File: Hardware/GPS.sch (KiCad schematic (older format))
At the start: 15 parts, among them Q1 IRLML6401, U1 ANTENOVA-UB

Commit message: Prepare for r2
Delete board, netlist, associations
Clear annotations
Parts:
- renumbered C7 to C?, C2 to C?, C1 to C?, C3 to C?, C5 to C?, C4 to C?, C6 to C?, FB1 to FB?, FB2 to FB?, L1 to L?, L2 to L?, Q1 to Q?, R4 to R?, R3 to R?, U1 to U?
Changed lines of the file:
@@
 $EndDescr
 $Comp
-L ANTENOVA-UB U1
+L ANTENOVA-UB U?
 U 1 1 52E9B1BE
 P 7100 4150
-F 0 "U1" H 7100 5300 60  0000 C CNN
+F 0 "U?" H 7100 5300 60  0000 C CNN
 F 1 "ANTENOVA-UB" H 7100 3000 60  0000 C CNN
 F 2 "~" H 7100 4150 60  0000 C CNN
@@
 $EndComp
 $Comp
-L C C7
+L C C?
 U 1 1 52E9B2C1
 P 7900 3450
-F 0 "C7" H 7950 3600 60  0000 L CNN
+F 0 "C?" H 7950 3600 60  0000 L CNN
 F 1 "18pF" H 7950 3300 60  0000 L CNN
 F 2 "CAPC1005-N" H 7900 3450 60  0001 C CNN
@@
 $EndComp
 $Comp
-L L L1
+L L L?
 U 1 1 52E9B2DC
 P 8350 3100
-F 0 "L1" H 8350 3000 60  0000 C CNN
+F 0 "L?" H 8350 3000 60  0000 C CNN
 F 1 "DNP" H 8350 3150 60  0000 C CNN
 F 2 "INDC1005-N" H 8350 3100 60  0001 C CNN
@@
 $EndComp
 $Comp
-L GND #PWR055
+L GND #PWR?
 U 1 1 52E9B2FA
 P 8700 3100
-F 0 "#PWR055" H 8700 3100 30  0001 C CNN
+F 0 "#PWR?" H 8700 3100 30  0001 C CNN
 F 1 "GND" H 8700 3030 30  0001 C CNN
 F 2 "" H 8700 3100 60  0000 C CNN
@@
 $EndComp
 $Comp
-L GND #PWR056
+L GND #PWR?
 U 1 1 52E9B317
 P 8700 3800
-F 0 "#PWR056" H 8700 3800 30  0001 C CNN
+F 0 "#PWR?" H 8700 3800 30  0001 C CNN
 F 1 "GND" H 8700 3730 30  0001 C CNN
 F 2 "" H 8700 3800 60  0000 C CNN
@@
 $EndComp
 $Comp
-L GND #PWR057
+L GND #PWR?
 U 1 1 52E9B346
 P 7800 5300
-F 0 "#PWR057" H 7800 5300 30  0001 C CNN
+F 0 "#PWR?" H 7800 5300 30  0001 C CNN
 F 1 "GND" H 7800 5230 30  0001 C CNN
 F 2 "" H 7800 5300 60  0000 C CNN
@@
 NoConn ~ 6500 3800
 $Comp
-L GND #PWR058
+L GND #PWR?
 U 1 1 52E9B409
 P 6400 5300
-F 0 "#PWR058" H 6400 5300 30  0001 C CNN
+F 0 "#PWR?" H 6400 5300 30  0001 C CNN
 F 1 "GND" H 6400 5230 30  0001 C CNN
 F 2 "" H 6400 5300 60  0000 C CNN
@@
 $EndComp
 $Comp
-L FERRITE FB1
+L FERRITE FB?
 U 1 1 52E9B435
 P 5150 4200
-F 0 "FB1" H 5100 4250 60  0000 R CNN
+F 0 "FB?" H 5100 4250 60  0000 R CNN
 F 1 "1k" H 5200 4150 60  0000 L CNN
 F 2 "RESC1005-N" H 5150 4200 60  0001 C CNN
@@
 $EndComp
 $Comp
-L FERRITE FB2
+L FERRITE FB?
 U 1 1 52E9B565
 P 5150 4500
-F 0 "FB2" H 5100 4550 60  0000 R CNN
+F 0 "FB?" H 5100 4550 60  0000 R CNN
 F 1 "1k" H 5200 4450 60  0000 L CNN
 F 2 "RESC1005-N" H 5150 4500 60  0001 C CNN
@@
 Connection ~ 6400 3300
 $Comp
-L C C2
+L C C?
 U 1 1 52E9B693
 P 5300 3550
-F 0 "C2" H 5350 3700 60  0000 L CNN
+F 0 "C?" H 5350 3700 60  0000 L CNN
 F 1 "22pF" H 5350 3400 60  0000 L CNN
 F 2 "CAPC1005-N" H 5300 3550 60  0001 C CNN
@@
 Connection ~ 6100 4400
 $Comp
-L GND #PWR059
+L GND #PWR?
 U 1 1 52E9B758
 P 5700 5200
-F 0 "#PWR059" H 5700 5200 30  0001 C CNN
+F 0 "#PWR?" H 5700 5200 30  0001 C CNN
 F 1 "GND" H 5700 5130 30  0001 C CNN
 F 2 "" H 5700 5200 60  0000 C CNN
@@
 $EndComp
 $Comp
-L GND #PWR060
+L GND #PWR?
 U 1 1 52E9B767
 P 6100 5200
-F 0 "#PWR060" H 6100 5200 30  0001 C CNN
+F 0 "#PWR?" H 6100 5200 30  0001 C CNN
 F 1 "GND" H 6100 5130 30  0001 C CNN
 F 2 "" H 6100 5200 60  0000 C CNN
@@
 	4900 4500 4700 4500
 $Comp
-L GND #PWR061
+L GND #PWR?
 U 1 1 52E9B83C
 P 5700 4000
-F 0 "#PWR061" H 5700 4000 30  0001 C CNN
+F 0 "#PWR?" H 5700 4000 30  0001 C CNN
 F 1 "GND" H 5700 3930 30  0001 C CNN
 F 2 "" H 5700 4000 60  0000 C CNN
@@
 $EndComp
 $Comp
-L GND #PWR062
+L GND #PWR?
 U 1 1 52E9B84B
 P 5300 3900
-F 0 "#PWR062" H 5300 3900 30  0001 C CNN
+F 0 "#PWR?" H 5300 3900 30  0001 C CNN
 F 1 "GND" H 5300 3830 30  0001 C CNN
 F 2 "" H 5300 3900 60  0000 C CNN
@@
 GPS_En
 $Comp
-L GND #PWR063
+L GND #PWR?
 U 1 1 52ECD7A8
 P 6100 4200
-F 0 "#PWR063" H 6100 4200 30  0001 C CNN
+F 0 "#PWR?" H 6100 4200 30  0001 C CNN
 F 1 "GND" H 6100 4130 30  0001 C CNN
 F 2 "" H 6100 4200 60  0000 C CNN
@@
 	6100 3000 6100 3600
 $Comp
-L +3.3V #PWR064
+L +3.3V #PWR?
 U 1 1 52ECD869
 P 6100 3000
-F 0 "#PWR064" H 6100 2960 30  0001 C CNN
+F 0 "#PWR?" H 6100 2960 30  0001 C CNN
 F 1 "+3.3V" H 6100 3110 30  0000 C CNN
 F 2 "" H 6100 3000 60  0000 C CNN
@@
 	5300 3100 5300 3300
 $Comp
-L MOSFET-P Q1
+L MOSFET-P Q?
 U 1 1 52EF2A40
 P 4300 3200
-F 0 "Q1" H 4200 3150 60  0000 R CNN
+F 0 "Q?" H 4200 3150 60  0000 R CNN
 F 1 "IRLML6401" V 4500 3200 60  0000 C CNN
 F 2 "SOT95P280-3N-GDS" H 4300 3200 60  0001 C CNN
@@
 $EndComp
 $Comp
-L GND #PWR065
+L GND #PWR?
 U 1 1 52EF2A9A
 P 4900 3800
-F 0 "#PWR065" H 4900 3800 30  0001 C CNN
+F 0 "#PWR?" H 4900 3800 30  0001 C CNN
 F 1 "GND" H 4900 3730 30  0001 C CNN
 F 2 "" H 4900 3800 60  0000 C CNN
@@
 Connection ~ 3500 3500
 $Comp
-L +3.3V #PWR066
+L +3.3V #PWR?
 U 1 1 52EF2CCE
 P 3500 2700
-F 0 "#PWR066" H 3500 2660 30  0001 C CNN
+F 0 "#PWR?" H 3500 2660 30  0001 C CNN
 F 1 "+3.3V" H 3500 2810 30  0000 C CNN
 F 2 "" H 3500 2700 60  0000 C CNN
@@
 Connection ~ 3500 2800
 $Comp
-L C C1
+L C C?
 U 1 1 52EF664A
 P 4900 3450
-F 0 "C1" H 4950 3600 60  0000 L CNN
+F 0 "C?" H 4950 3600 60  0000 L CNN
 F 1 "4.7uF" H 4950 3300 60  0000 L CNN
 F 2 "CAPC2012-N" H 4900 3450 60  0001 C CNN
@@
 $EndComp
 $Comp
-L C C3
+L C C?
 U 1 1 52EF6821
 P 5700 3650
-F 0 "C3" H 5750 3800 60  0000 L CNN
+F 0 "C?" H 5750 3800 60  0000 L CNN
 F 1 "22pF" H 5750 3500 60  0000 L CNN
 F 2 "CAPC1005-N" H 5700 3650 60  0001 C CNN
@@
 $EndComp
 $Comp
-L C C5
+L C C?
 U 1 1 52EF682C
 P 6100 3850
-F 0 "C5" H 6150 4000 60  0000 L CNN
+F 0 "C?" H 6150 4000 60  0000 L CNN
 F 1 "22pF" H 6150 3700 60  0000 L CNN
 F 2 "CAPC1005-N" H 6100 3850 60  0001 C CNN
@@
 $EndComp
 $Comp
-L C C4
+L C C?
 U 1 1 52EF6837
 P 5700 4850
-F 0 "C4" H 5750 5000 60  0000 L CNN
+F 0 "C?" H 5750 5000 60  0000 L CNN
 F 1 "22pF" H 5750 4700 60  0000 L CNN
 F 2 "CAPC1005-N" H 5700 4850 60  0001 C CNN
@@
 $EndComp
 $Comp
-L C C6
+L C C?
 U 1 1 52EF6842
 P 6100 4850
-F 0 "C6" H 6150 5000 60  0000 L CNN
+F 0 "C?" H 6150 5000 60  0000 L CNN
 F 1 "22pF" H 6150 4700 60  0000 L CNN
 F 2 "CAPC1005-N" H 6100 4850 60  0001 C CNN
@@
 $EndComp
 $Comp
-L L L2
+L L L?
 U 1 1 52EF6969
 P 8350 3800
-F 0 "L2" H 8350 3700 60  0000 C CNN
+F 0 "L?" H 8350 3700 60  0000 C CNN
 F 1 "DNP" H 8350 3850 60  0000 C CNN
 F 2 "INDC1005-N" H 8350 3800 60  0001 C CNN
@@
 $EndComp
 $Comp
-L R R4
+L R R?
 U 1 1 530ACEAC
 P 3850 3500
-F 0 "R4" H 3850 3600 50  0000 C CNN
+F 0 "R?" H 3850 3600 50  0000 C CNN
 F 1 "120" H 3850 3500 50  0000 C CNN
 F 2 "RESC1005_N" H 3850 3500 60  0001 C CNN
@@
 $EndComp
 $Comp
-L R R3
+L R R?
 U 1 1 530ADB7A
 P 3500 3150
-F 0 "R3" H 3500 3250 50  0000 C CNN
+F 0 "R?" H 3500 3250 50  0000 C CNN
 F 1 "10k" H 3500 3150 50  0000 C CNN
 F 2 "RESC1005-N" H 3500 3150 60  0001 C CNN

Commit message: Prepare for new GPS
Remove connections to subsheet
Clear subsheet
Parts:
- removed C?: 18pF, CAPC1005-N, symbol C
- removed C? (x5): 22pF, CAPC1005-N, symbol C
- removed C?: 4.7uF, CAPC2012-N, symbol C
- removed FB? (x2): 1k, RESC1005-N, symbol FERRITE
- removed L? (x2): DNP, INDC1005-N, symbol L
- removed Q?: IRLML6401, SOT95P280-3N-GDS, symbol MOSFET-P
- removed R?: 120, RESC1005_N, symbol R
- removed R?: 10k, RESC1005-N, symbol R
- removed U?: ANTENOVA-UB, ~, symbol ANTENOVA-UB
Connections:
- net labels removed: +3.3V, GND, GPS_En, GPS_Perf, RX, TX
- wire segments 55 -> 0
- no-connect marks 13 -> 0

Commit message: Add Venus838 to schematic
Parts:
- added AE?: ANTENNA, ~, symbol ANTENNA
- added C? (x3): 1uF, ~, symbol C
- added L?: DNP, ~, symbol L
- added R?: 33k, ~, symbol R
- added R?: DNP, ~, symbol R
- added U?: VENUS838FLPX-L, ~, symbol VENUS838FLPX-L
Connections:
- new net: C?.1, R?.1, U?.1 (RSTN)
- new net: C?.1, U?.18 (VBAT)
- new net: C?.1, R?.2, U?.2 (VCC), U?.36 (REGEN)
- new net: AE?.P, L?.2, U?.32 (RFIN)
- new net: R?.1, U?.9 (BOOT)
- new net GND: AE?.S, C?.2, C?.2, C?.2, L?.1, U?.10 (GND), U?.11 (GND), U?.14 (BAUD1), U?.15 (GND), U?.19 (GND), U?.21 (RFGND), U?.22 (RFGND), U?.24 (RFGND), U?.25 (RFGND), U?.27 (RFGND), U?.28 (RFGND), U?.29 (RFGND), U?.31 (RFGND), U?.33 (RFGND), U?.37 (BAUD0), U?.4 (GND), U?.5 (GND), U?.6 (GND)
- new net GPS_DI: U?.42 (RX)
- new net GPS_DO: U?.44 (TX)
- new net GPS_LED: U?.7 (LED)
- new net GPS_PPS: U?.40 (PPS)
- no-connect marks 0 -> 1

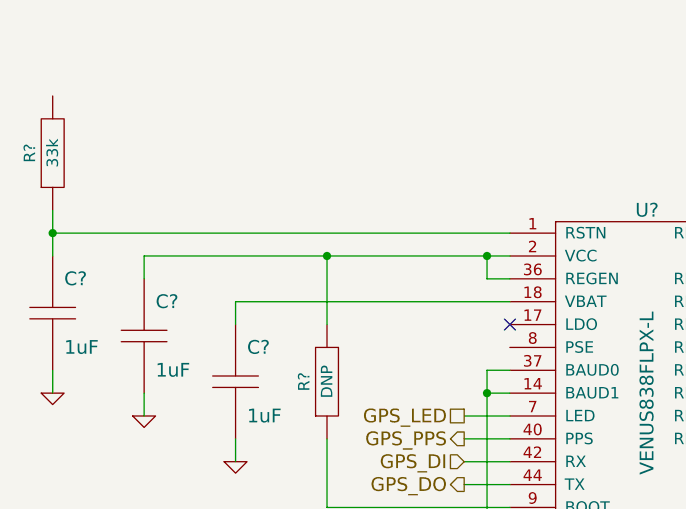
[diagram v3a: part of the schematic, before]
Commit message: Connect GPS power
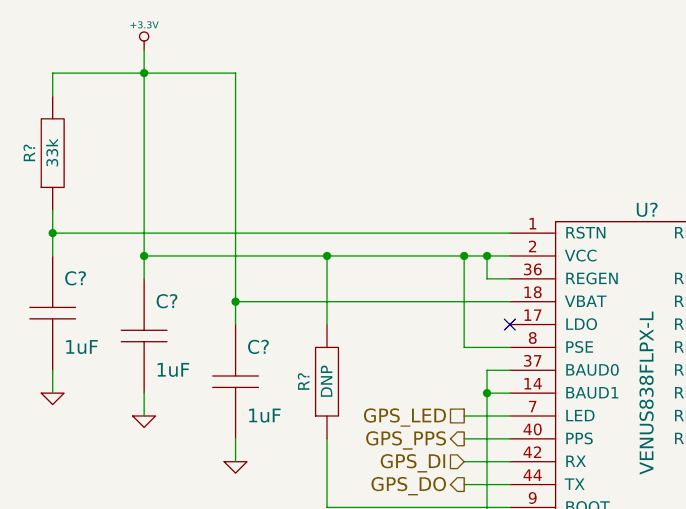
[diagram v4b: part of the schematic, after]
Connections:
- net +3.3V: now reaches C?.1, U?.18 (VBAT)
- net +3.3V: now also C?.1, R?.2, R?.2, U?.2 (VCC), U?.36 (REGEN), U?.8 (PSE)
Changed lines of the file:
@@
 $EndComp
 Wire Wire Line
-	3800 3500 3800 3400
+	3800 2500 3800 3500
 Wire Wire Line
 	3800 3400 5400 3400
@@
 $EndComp
 Wire Wire Line
-	4200 3700 4200 3600
+	4200 2600 4200 3700
 Wire Wire Line
 	4200 3600 5400 3600
@@
 	4600 3700 4600 3400
 Connection ~ 4600 3400
+$Comp
+L +3.3V #PWR?
+U 1 1 53B0965B
+P 3800 2500
+F 0 "#PWR?" H 3800 2460 30  0001 C CNN
+F 1 "+3.3V" H 3800 2610 30  0000 C CNN
+F 2 "" H 3800 2500 60  0000 C CNN
+F 3 "" H 3800 2500 60  0000 C CNN
+	1    3800 2500
+	1    0    0    -1
+$EndComp
+Connection ~ 3800 3400
+Wire Wire Line
+	3400 2700 3400 2600
+Wire Wire Line
+	3400 2600 4200 2600
+Connection ~ 3800 2600
+Connection ~ 4200 3600
+Wire Wire Line
+	5400 3800 5200 3800
+Wire Wire Line
+	5200 3800 5200 3400
+Connection ~ 5200 3400
 $EndSCHEMATC

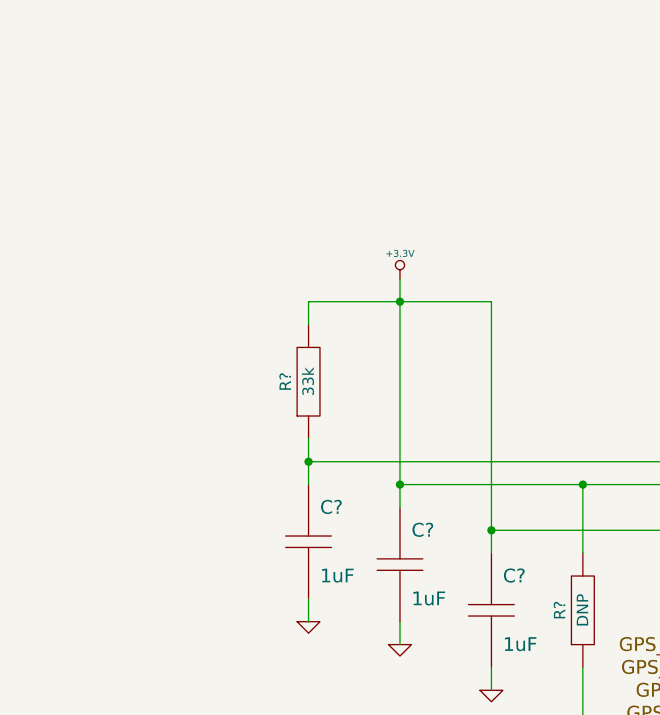
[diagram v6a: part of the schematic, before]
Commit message: Add GPS load switch
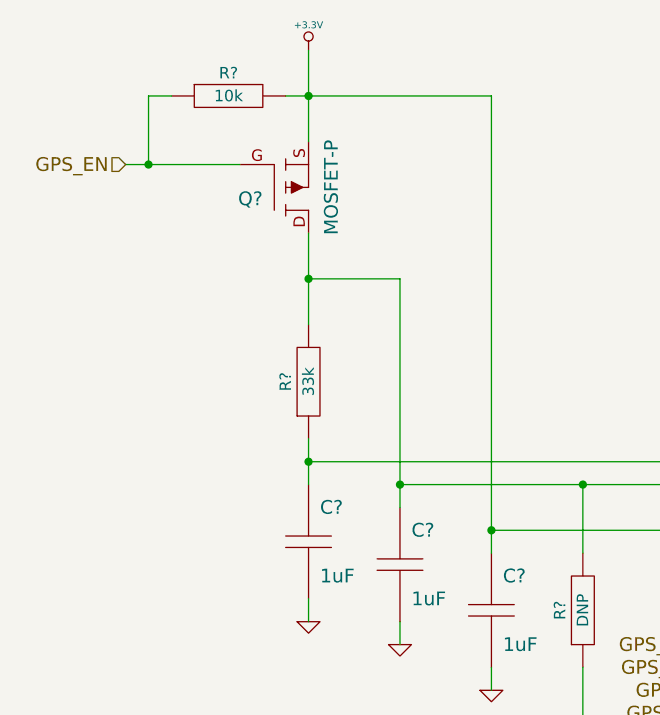
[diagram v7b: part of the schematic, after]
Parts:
- added Q?: MOSFET-P, ~, symbol MOSFET-P
- added R?: 10k, ~, symbol R
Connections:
- net +3.3V: now also Q?.S, R?.2; no longer C?.1, R?.2, R?.2, U?.2 (VCC), U?.36 (REGEN), U?.8 (PSE)
- new net: C?.1, Q?.D, R?.2, R?.2, U?.2 (VCC), U?.36 (REGEN), U?.8 (PSE)
- new net GPS_EN: Q?.G, R?.1
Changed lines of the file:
@@
 $Descr A4 11693 8268
 encoding utf-8
-Sheet 4 4
+Sheet 3 5
 Title "Aether - Pico Tracker"
-Date "30 jul 2014"
+Date "2 aug 2014"
 Rev "1"
 Comp "Aerodyne Labs"
@@
 $EndComp
 Wire Wire Line
-	3800 2500 3800 3500
-Wire Wire Line
 	3800 3400 5400 3400
 Wire Wire Line
@@
 	1    0    0    -1
 $EndComp
-Wire Wire Line
-	4200 2600 4200 3700
 Wire Wire Line
 	4200 3600 5400 3600
@@
 L +3.3V #PWR?
 U 1 1 53B0965B
-P 3800 2500
-F 0 "#PWR?" H 3800 2460 30  0001 C CNN
-F 1 "+3.3V" H 3800 2610 30  0000 C CNN
-F 2 "" H 3800 2500 60  0000 C CNN
-F 3 "" H 3800 2500 60  0000 C CNN
-	1    3800 2500
-	1    0    0    -1
-$EndComp
-Connection ~ 3800 3400
-Wire Wire Line
-	3400 2700 3400 2600
-Wire Wire Line
-	3400 2600 4200 2600
-Connection ~ 3800 2600
+P 3400 1500
+F 0 "#PWR?" H 3400 1460 30  0001 C CNN
+F 1 "+3.3V" H 3400 1610 30  0000 C CNN
+F 2 "" H 3400 1500 60  0000 C CNN
+F 3 "" H 3400 1500 60  0000 C CNN
+	1    3400 1500
+	1    0    0    -1
+$EndComp
 Connection ~ 4200 3600
 Wire Wire Line
@@
 	5200 3800 5200 3400
 Connection ~ 5200 3400
+$Comp
+L MOSFET-P Q?
+U 1 1 53DC7561
+P 3300 2100
+F 0 "Q?" H 3200 2050 60  0000 R CNN
+F 1 "MOSFET-P" V 3500 2100 60  0000 C CNN
+F 2 "~" H 3300 2100 60  0000 C CNN
+F 3 "~" H 3300 2100 60  0000 C CNN
+	1    3300 2100
+	1    0    0    -1
+$EndComp
+Wire Wire Line
+	3400 2300 3400 2700
+Wire Wire Line
+	3800 2500 3800 3500
+Wire Wire Line
+	3800 2500 3400 2500
+Connection ~ 3400 2500
+Connection ~ 3800 3400
+Wire Wire Line
+	4200 1700 4200 3700
+Wire Wire Line
+	3400 1500 3400 1900
+Wire Wire Line
+	3300 1700 4200 1700
+Connection ~ 3400 1700
+$Comp
+L R R?
+U 1 1 53DC774B
+P 3050 1700
+F 0 "R?" H 3050 1800 50  0000 C CNN
+F 1 "10k" H 3050 1700 50  0000 C CNN
+F 2 "~" H 3050 1700 60  0000 C CNN
+F 3 "~" H 3050 1700 60  0000 C CNN
+F 4 "W" H 3050 1600 50  0001 C CNN "Power"
+F 5 "%" H 3050 1500 50  0001 C CNN "Tolerance"
+	1    3050 1700
+	1    0    0    -1
+$EndComp
+Text HLabel 2600 2000 0    60   Input ~ 0
+GPS_EN
+Wire Wire Line
+	2600 2000 3100 2000
+Wire Wire Line
+	2800 1700 2700 1700
+Wire Wire Line
+	2700 1700 2700 2000
+Connection ~ 2700 2000
 $EndSCHEMATC
